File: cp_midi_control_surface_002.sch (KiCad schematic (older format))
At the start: 23 parts, among them P1 Power, P2 Analogue, P3 Digital, P4 Communication, P5 PWM, P6 PWM

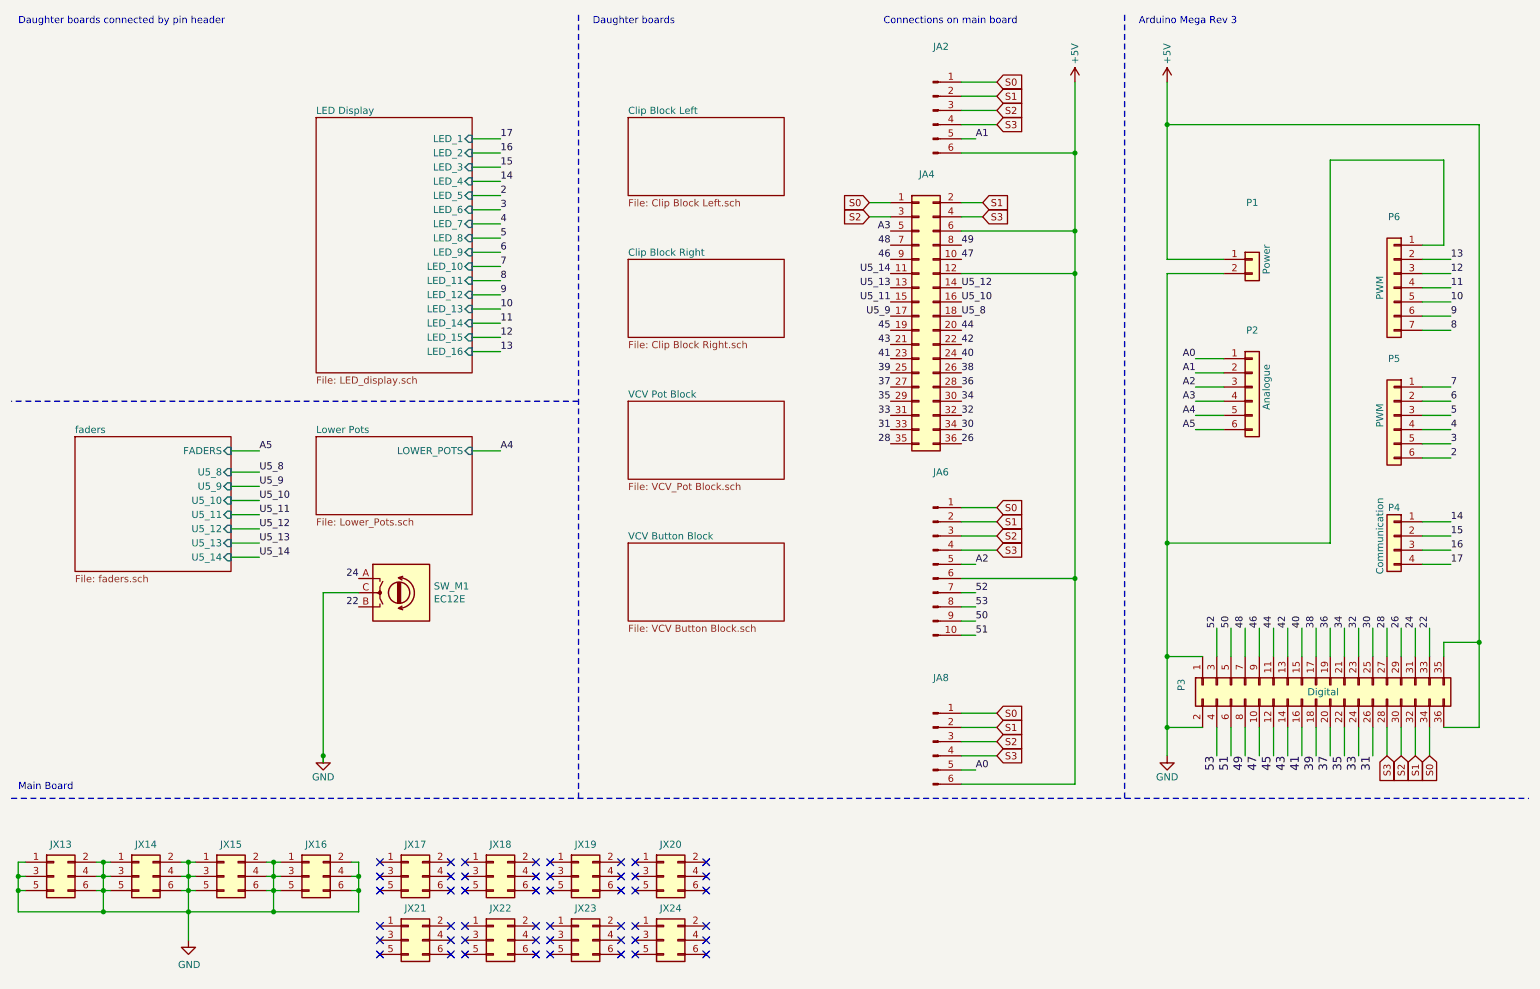
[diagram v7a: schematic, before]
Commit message: Rails done, GND corrected.
Now for checking and decals
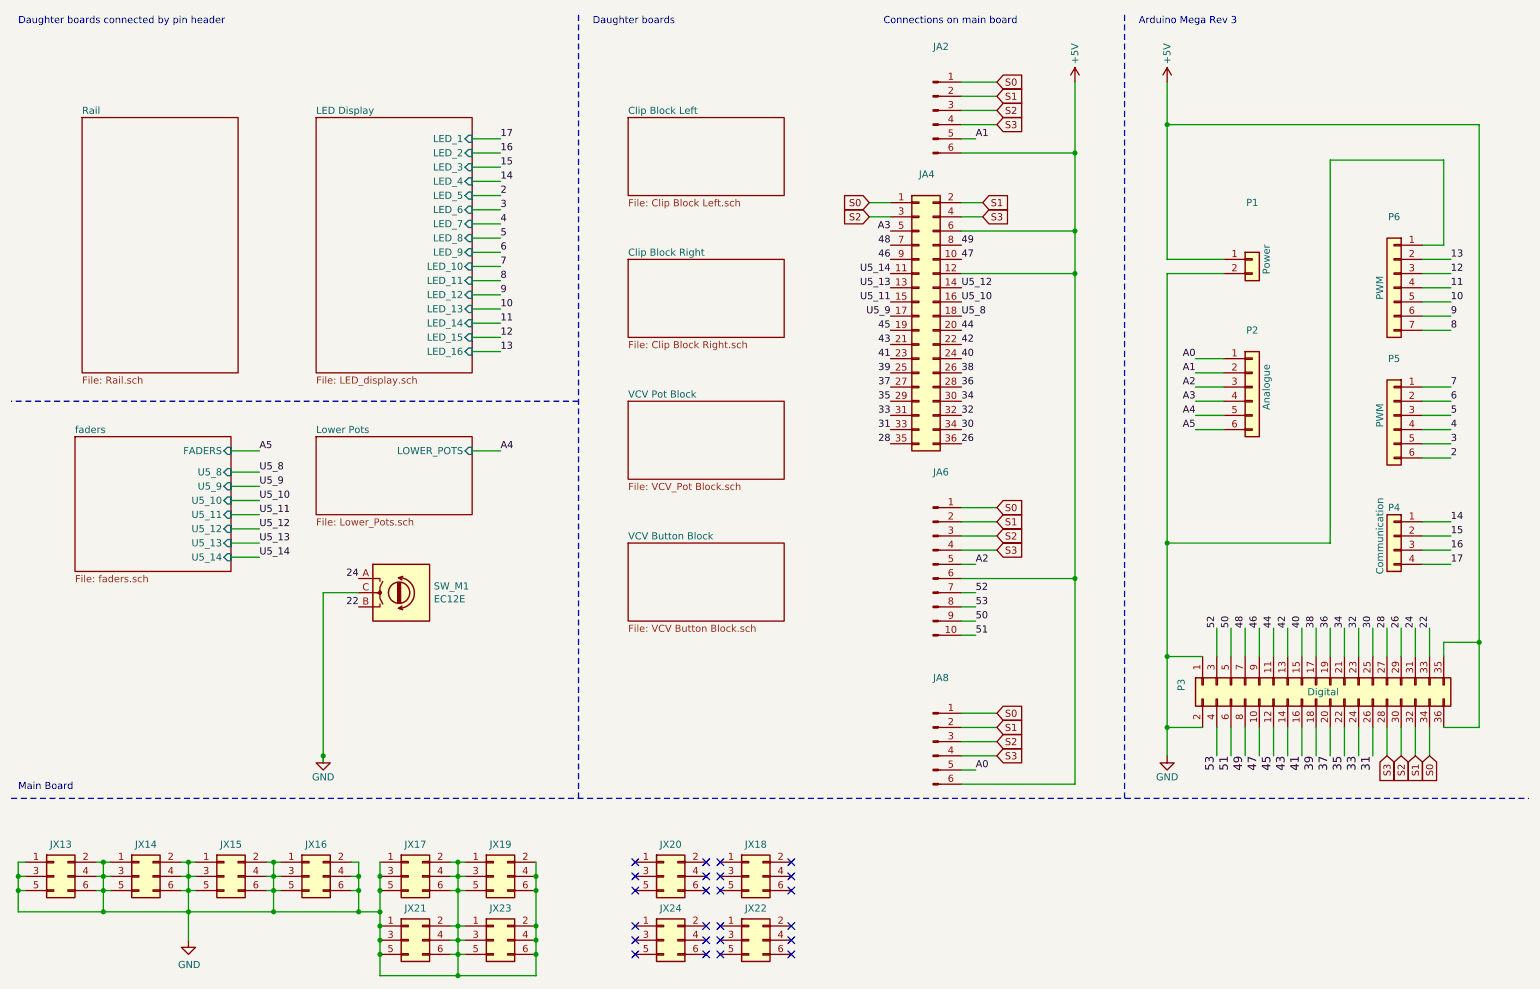
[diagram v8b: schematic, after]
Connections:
- net GND: now also JX17.1 (Pin_1), JX17.2 (Pin_2), JX17.3 (Pin_3), JX17.4 (Pin_4), JX17.5 (Pin_5), JX17.6 (Pin_6), JX19.1 (Pin_1), JX19.2 (Pin_2), JX19.3 (Pin_3), JX19.4 (Pin_4), JX19.5 (Pin_5), JX19.6 (Pin_6), JX21.1 (Pin_1), JX21.2 (Pin_2), JX21.3 (Pin_3), JX21.4 (Pin_4), JX21.5 (Pin_5), JX21.6 (Pin_6), JX23.1 (Pin_1), JX23.2 (Pin_2), JX23.3 (Pin_3), JX23.4 (Pin_4), JX23.5 (Pin_5), JX23.6 (Pin_6)
- no-connect marks 48 -> 24
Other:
- moved on the sheet: JX18, JX19, JX22, JX23
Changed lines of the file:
@@
 $Descr A4 11693 8268
 encoding utf-8
-Sheet 1 8
+Sheet 1 9
 Title "cp_midi_controller_002"
 Date "2019-01-13"
@@
 L Connector_Generic:Conn_02x03_Odd_Even JX?
 U 1 1 5D998042
-P 3900 6600
+P 5700 6600
 AR Path="/5C4B73B3/5D998042" Ref="JX?"  Part="1"
 AR Path="/5D998042" Ref="JX18"  Part="1"
-F 0 "JX18" H 3950 6825 50  0000 C CNN
+F 0 "JX18" H 5750 6825 50  0000 C CNN
+F 1 "Conn_02x03_Odd_Even" H 5750 6826 50  0001 C CNN
+F 2 "Connector_PinHeader_2.54mm:PinHeader_2x03_P2.54mm_Vertical" H 5700 6600 50  0001 C CNN
+F 3 "~" H 5700 6600 50  0001 C CNN
+	1    5700 6600
+	1    0    0    -1
+$EndComp
+NoConn ~ 6000 6500
+NoConn ~ 6000 6600
+NoConn ~ 6000 6700
+NoConn ~ 5500 6500
+NoConn ~ 5500 6600
+NoConn ~ 5500 6700
+$Comp
+L Connector_Generic:Conn_02x03_Odd_Even JX?
+U 1 1 5D99F050
+P 3900 6600
+AR Path="/5C4B73B3/5D99F050" Ref="JX?"  Part="1"
+AR Path="/5D99F050" Ref="JX19"  Part="1"
+F 0 "JX19" H 3950 6825 50  0000 C CNN
 F 1 "Conn_02x03_Odd_Even" H 3950 6826 50  0001 C CNN
 F 2 "Connector_PinHeader_2.54mm:PinHeader_2x03_P2.54mm_Vertical" H 3900 6600 50  0001 C CNN
@@
 	1    0    0    -1
 $EndComp
-NoConn ~ 4200 6500
-NoConn ~ 4200 6600
-NoConn ~ 4200 6700
-NoConn ~ 3700 6500
-NoConn ~ 3700 6600
-NoConn ~ 3700 6700
-$Comp
-L Connector_Generic:Conn_02x03_Odd_Even JX?
-U 1 1 5D99F050
-P 4500 6600
-AR Path="/5C4B73B3/5D99F050" Ref="JX?"  Part="1"
-AR Path="/5D99F050" Ref="JX19"  Part="1"
-F 0 "JX19" H 4550 6825 50  0000 C CNN
-F 1 "Conn_02x03_Odd_Even" H 4550 6826 50  0001 C CNN
-F 2 "Connector_PinHeader_2.54mm:PinHeader_2x03_P2.54mm_Vertical" H 4500 6600 50  0001 C CNN
-F 3 "~" H 4500 6600 50  0001 C CNN
-	1    4500 6600
-	1    0    0    -1
-$EndComp
-NoConn ~ 4800 6500
-NoConn ~ 4800 6600
-NoConn ~ 4800 6700
-NoConn ~ 4300 6500
-NoConn ~ 4300 6600
-NoConn ~ 4300 6700
 $Comp
 L Connector_Generic:Conn_02x03_Odd_Even JX?
@@
 	1    0    0    -1
 $EndComp
-NoConn ~ 3600 6500
-NoConn ~ 3600 6600
-NoConn ~ 3600 6700
-NoConn ~ 3100 6500
-NoConn ~ 3100 6600
-NoConn ~ 3100 6700
 $Comp
 L Connector_Generic:Conn_02x03_Odd_Even JX?
@@
 L Connector_Generic:Conn_02x03_Odd_Even JX?
 U 1 1 5D9BB262
-P 3900 7050
+P 5700 7050
 AR Path="/5C4B73B3/5D9BB262" Ref="JX?"  Part="1"
 AR Path="/5D9BB262" Ref="JX22"  Part="1"
-F 0 "JX22" H 3950 7275 50  0000 C CNN
+F 0 "JX22" H 5750 7275 50  0000 C CNN
+F 1 "Conn_02x03_Odd_Even" H 5750 7276 50  0001 C CNN
+F 2 "Connector_PinHeader_2.54mm:PinHeader_2x03_P2.54mm_Vertical" H 5700 7050 50  0001 C CNN
+F 3 "~" H 5700 7050 50  0001 C CNN
+	1    5700 7050
+	1    0    0    -1
+$EndComp
+NoConn ~ 6000 6950
+NoConn ~ 6000 7050
+NoConn ~ 6000 7150
+NoConn ~ 5500 6950
+NoConn ~ 5500 7050
+NoConn ~ 5500 7150
+$Comp
+L Connector_Generic:Conn_02x03_Odd_Even JX?
+U 1 1 5D9BB26F
+P 3900 7050
+AR Path="/5C4B73B3/5D9BB26F" Ref="JX?"  Part="1"
+AR Path="/5D9BB26F" Ref="JX23"  Part="1"
+F 0 "JX23" H 3950 7275 50  0000 C CNN
 F 1 "Conn_02x03_Odd_Even" H 3950 7276 50  0001 C CNN
 F 2 "Connector_PinHeader_2.54mm:PinHeader_2x03_P2.54mm_Vertical" H 3900 7050 50  0001 C CNN
@@
 	1    0    0    -1
 $EndComp
-NoConn ~ 4200 6950
-NoConn ~ 4200 7050
-NoConn ~ 4200 7150
-NoConn ~ 3700 6950
-NoConn ~ 3700 7050
-NoConn ~ 3700 7150
-$Comp
-L Connector_Generic:Conn_02x03_Odd_Even JX?
-U 1 1 5D9BB26F
-P 4500 7050
-AR Path="/5C4B73B3/5D9BB26F" Ref="JX?"  Part="1"
-AR Path="/5D9BB26F" Ref="JX23"  Part="1"
-F 0 "JX23" H 4550 7275 50  0000 C CNN
-F 1 "Conn_02x03_Odd_Even" H 4550 7276 50  0001 C CNN
-F 2 "Connector_PinHeader_2.54mm:PinHeader_2x03_P2.54mm_Vertical" H 4500 7050 50  0001 C CNN
-F 3 "~" H 4500 7050 50  0001 C CNN
-	1    4500 7050
-	1    0    0    -1
-$EndComp
-NoConn ~ 4800 6950
-NoConn ~ 4800 7050
-NoConn ~ 4800 7150
-NoConn ~ 4300 6950
-NoConn ~ 4300 7050
-NoConn ~ 4300 7150
 $Comp
 L Connector_Generic:Conn_02x03_Odd_Even JX?
@@
 	1    0    0    -1
 $EndComp
-NoConn ~ 3600 6950
-NoConn ~ 3600 7050
-NoConn ~ 3600 7150
-NoConn ~ 3100 6950
-NoConn ~ 3100 7050
-NoConn ~ 3100 7150
 $Comp
 L Connector_Generic:Conn_02x03_Odd_Even JX?
@@
 Wire Wire Line
 	2050 4350 2250 4350
+$Sheet
+S 1000 1250 1100 1800
+U 5D622E10
+F0 "Rail" 50
+F1 "Rail.sch" 50
+$EndSheet
+Wire Wire Line
+	2950 6850 3100 6850
+Wire Wire Line
+	3100 6850 3100 6700
+Connection ~ 2950 6850
+Connection ~ 3100 6600
+Wire Wire Line
+	3100 6600 3100 6500
+Connection ~ 3100 6700
+Wire Wire Line
+	3100 6700 3100 6600
+Wire Wire Line
+	3100 6850 3100 6950
+Connection ~ 3100 6850
+Connection ~ 3100 6950
+Wire Wire Line
+	3100 6950 3100 7050
+Connection ~ 3100 7050
+Wire Wire Line
+	3650 6500 3650 6600
+Wire Wire Line
+	3650 7300 3100 7300
+Wire Wire Line
+	3100 7050 3100 7150
+Connection ~ 3100 7150
+Wire Wire Line
+	3100 7150 3100 7300
+Wire Wire Line
+	3600 6500 3650 6500
+Connection ~ 3650 6500
+Wire Wire Line
+	3650 6500 3700 6500
+Wire Wire Line
+	3600 6600 3650 6600
+Wire Wire Line
+	3600 6700 3650 6700
+Wire Wire Line
+	3600 6950 3650 6950
+Connection ~ 3650 6950
+Wire Wire Line
+	3650 6950 3650 7050
+Wire Wire Line
+	3700 6950 3650 6950
+Wire Wire Line
+	3600 7050 3650 7050
+Connection ~ 3650 7050
+Wire Wire Line
+	3650 7050 3650 7150
+Wire Wire Line
+	3700 7050 3650 7050
+Wire Wire Line
+	3600 7150 3650 7150
+Connection ~ 3650 7150
+Wire Wire Line
+	3650 7150 3650 7300
+Wire Wire Line
+	3650 7150 3700 7150
+Connection ~ 3650 6700
+Wire Wire Line
+	3650 6700 3650 6950
+Wire Wire Line
+	3650 6700 3700 6700
+Connection ~ 3650 6600
+Wire Wire Line
+	3650 6600 3650 6700
+Wire Wire Line
+	3650 6600 3700 6600
+Wire Wire Line
+	4200 6500 4200 6600
+Wire Wire Line
+	4200 7300 3650 7300
+Connection ~ 4200 6600
+Wire Wire Line
+	4200 6600 4200 6700
+Connection ~ 4200 6700
+Wire Wire Line
+	4200 6700 4200 6950
+Connection ~ 4200 6950
+Wire Wire Line
+	4200 6950 4200 7050
+Connection ~ 4200 7050
+Wire Wire Line
+	4200 7050 4200 7150
+Connection ~ 4200 7150
+Wire Wire Line
+	4200 7150 4200 7300
+Connection ~ 3650 7300
 $EndSCHEMATC
